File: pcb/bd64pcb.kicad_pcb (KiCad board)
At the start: 2 copper layers, 266.7 x 95.3 mm, 239 parts, among them J1 USB_C_Receptacle_USB2.0, J2 USB_B_Micro, SW1 SW_Push, U1 ATmega32U4-MU, U2 MCP23017_ML, U3 IS31FL3733-QF, Y1 16MHz

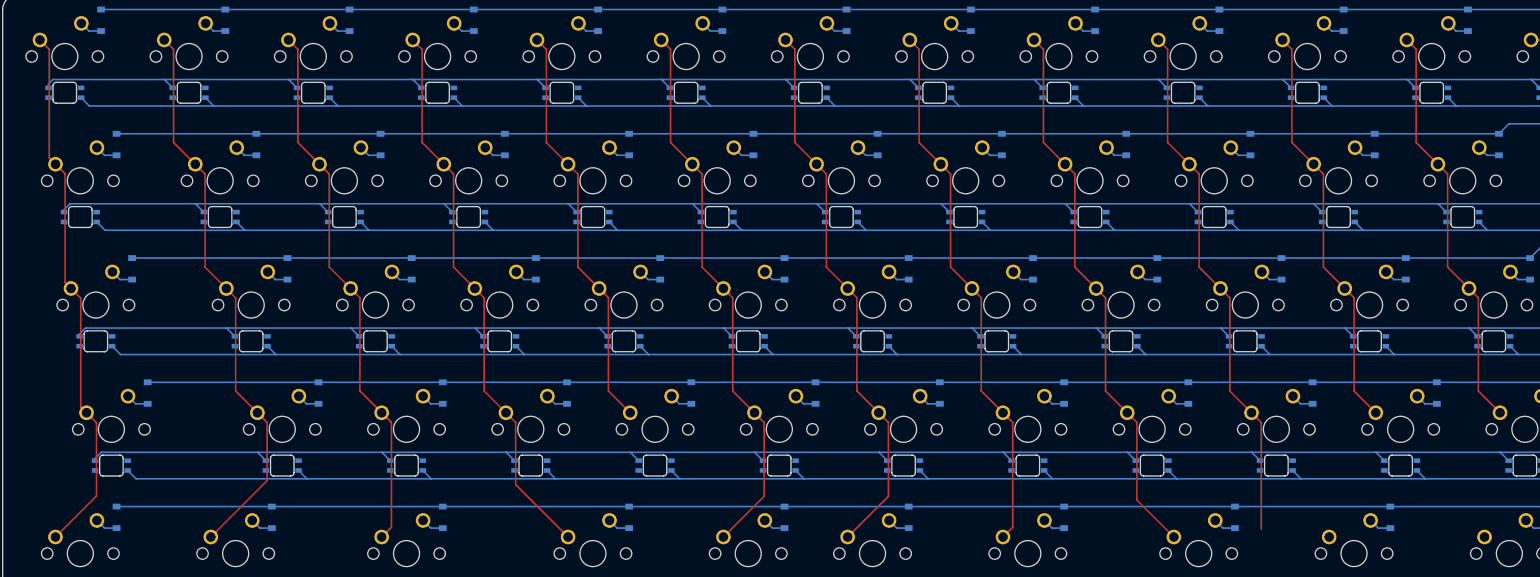
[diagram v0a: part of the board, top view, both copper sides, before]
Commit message: first non45 trace down
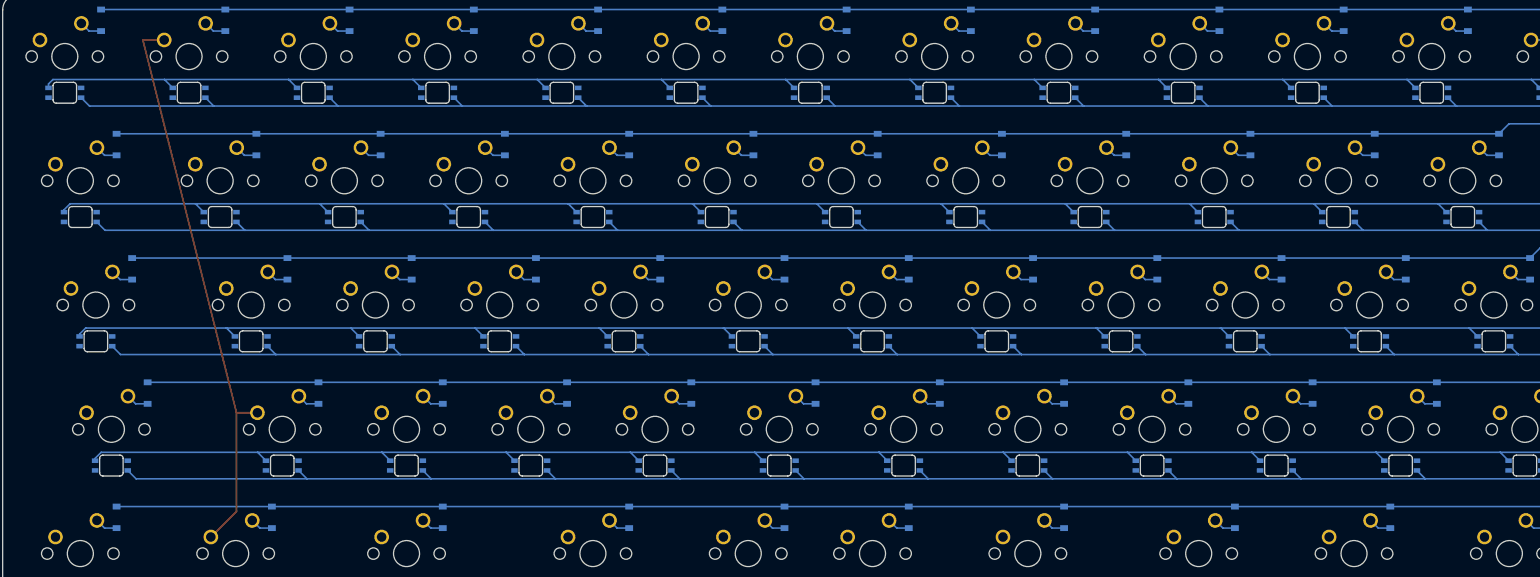
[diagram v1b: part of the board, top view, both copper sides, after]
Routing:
- net col3: track 86.1 -> 0.00 mm
- net col6: track 85.3 -> 0.00 mm
- net col5: track 85.3 -> 0.00 mm
- net col8: track 85.1 -> 0.00 mm
- net col2: track 83.4 -> 0.00 mm
- net col7: track 83.4 -> 0.00 mm
- net col0: track 82.4 -> 0.00 mm
- net col9: track 81.6 -> 0.00 mm
- net col10: track 63.1 -> 0.00 mm
- net col4: track 63.1 -> 0.00 mm
- net col11: track 63.1 -> 0.00 mm

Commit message: boring traces on most LEDs. updated to kicad 6
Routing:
- net col11: track 0.00 -> 102.1 mm, vias 0 -> 1
- net col10: track 0.00 -> 97.4 mm, vias 0 -> 1
- net col9: track 0.00 -> 92.6 mm, vias 0 -> 1
- net col3: track 0.00 -> 86.1 mm
- net col6: track 0.00 -> 85.2 mm
- net col5: track 0.00 -> 85.2 mm
- net col8: track 0.00 -> 85.1 mm
- net col7: track 0.00 -> 83.2 mm
- net col2: track 0.00 -> 83.2 mm
- net col0: track 0.00 -> 82.3 mm
- net CS9: track 0.00 -> 67.6 mm, vias 0 -> 4
- net CS7: track 0.00 -> 67.6 mm, vias 0 -> 4
- net CS12: track 0.00 -> 67.6 mm, vias 0 -> 4
- net CS10: track 0.00 -> 67.6 mm, vias 0 -> 4
- net CS5: track 0.00 -> 67.6 mm, vias 0 -> 4
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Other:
- board size 266.7 x 95.3 mm -> 266.7 x 95.2 mm
- net class Default removed
- net class Power removed

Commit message: still tracing LEDs
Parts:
- moved L48 209.4 mm to (198.4, 133.3)
- moved L47 202.3 mm to (172.2, 133.3)
- moved L46 197.6 mm to (148.4, 133.3)
- moved L32 152.7 mm to (129.4, 133.3)
- moved L31 148.1 mm to (105.6, 133.3)
- moved L30 138.8 mm to (77.0, 133.3)
- moved L16 74.1 mm to (50.8, 133.3)
- moved L15 72.3 mm to (27.0, 133.3)
- moved C9 14.4 mm to (52.8, 158.4), turned to -90 degrees
- moved JP6 13.2 mm to (52.8, 154.9), turned to 90 degrees
- moved C12 10.1 mm to (42.9, 159.1)
- moved C11 9.53 mm to (46.5, 159.1)
- moved C10 9.18 mm to (50.0, 159.1)
- moved C16 9.18 mm to (69.2, 184.2)
- moved C8 9.18 mm to (89.4, 155.1)
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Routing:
- net SW1: track 0.00 -> 286.7 mm, vias 0 -> 26
- net SW4: track 0.00 -> 274.9 mm, vias 0 -> 24
- net SW10: track 0.00 -> 274.9 mm, vias 0 -> 24
- net SW7: track 0.00 -> 274.2 mm, vias 0 -> 24
- net CS13: track 0.00 -> 44.6 mm, vias 0 -> 4

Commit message: shifted diodes over a tad
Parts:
- moved D61 6.51 mm to (197.5, 122.2)
- moved D62 6.51 mm to (221.3, 122.2)
- moved D63 6.51 mm to (245.1, 122.2)
- moved D64 6.51 mm to (268.9, 122.2)
- moved D10 6.35 mm to (195.3, 46.0)
- moved D14 6.35 mm to (271.5, 46.0)
- moved D25 6.35 mm to (219.1, 65.1)
- moved D34 6.35 mm to (147.6, 84.1)
- moved D39 6.35 mm to (242.9, 84.1)
- moved D40 6.35 mm to (266.7, 84.1)
- moved D48 6.35 mm to (171.4, 103.2)
- moved D59 6.35 mm to (147.6, 122.2)
- moved D60 6.35 mm to (171.4, 122.2)
- moved D17 6.35 mm to (66.7, 65.1)
- moved D18 6.35 mm to (85.7, 65.1)
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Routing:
- net row3: track 257.0 -> 216.8 mm, vias 2 -> 0
- net CS13: track 44.6 -> 74.5 mm, vias 4 -> 6
- net row4: track 265.2 -> 262.7 mm
- net row1: track 266.6 -> 264.6 mm
- net row2: track 257.0 -> 255.8 mm

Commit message: removed all traces. restarting
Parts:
- moved U1 126.0 mm to (44.0, 104.8), turned to 45 degrees
- moved F1 124.8 mm to (16.7, 31.0)
- moved JP1 122.8 mm to (24.4, 29.8)
- moved JP2 122.8 mm to (27.1, 29.8)
- moved R1 122.8 mm to (24.4, 33.2)
- moved R2 122.8 mm to (27.1, 33.2)
- moved J1 116.8 mm to (33.4, 46.4)
- moved U2 102.6 mm to (40.8, 85.7), turned to 45 degrees
- moved U3 54.3 mm to (91.3, 127.8), turned to 45 degrees
- moved R11 18.6 mm to (49.4, 153.7)
- moved C14 18.6 mm to (29.5, 153.7)
- moved C15 18.6 mm to (25.9, 153.7)
- moved C13 18.6 mm to (33.0, 153.7)
- moved JP7 18.6 mm to (47.9, 176.5)
- moved R10 18.6 mm to (54.9, 149.7)
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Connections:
- J1 pad A8: (no net) -> unconnected-(J1-PadA8)
- J1 pad B8: (no net) -> unconnected-(J1-PadB8)
- J2 pad 4: (no net) -> unconnected-(J2-Pad4)
- U1 pad 1: (no net) -> unconnected-(U1-Pad1)
- U1 pad 10: (no net) -> unconnected-(U1-Pad10)
- U1 pad 11: (no net) -> unconnected-(U1-Pad11)
- U1 pad 12: (no net) -> unconnected-(U1-Pad12)
- U1 pad 21: (no net) -> unconnected-(U1-Pad21)
- U1 pad 22: (no net) -> unconnected-(U1-Pad22)
- U1 pad 25: (no net) -> unconnected-(U1-Pad25)
- U1 pad 26: (no net) -> unconnected-(U1-Pad26)
- U1 pad 27: (no net) -> unconnected-(U1-Pad27)
- U1 pad 28: (no net) -> unconnected-(U1-Pad28)
- U1 pad 30: (no net) -> unconnected-(U1-Pad30)
- U1 pad 32: (no net) -> unconnected-(U1-Pad32)
- U1 pad 36: (no net) -> unconnected-(U1-Pad36)
- U1 pad 37: (no net) -> unconnected-(U1-Pad37)
- U1 pad 38: (no net) -> unconnected-(U1-Pad38)
- U1 pad 39: (no net) -> unconnected-(U1-Pad39)
- U1 pad 40: (no net) -> unconnected-(U1-Pad40)
- U1 pad 41: (no net) -> unconnected-(U1-Pad41)
- U1 pad 42: (no net) -> unconnected-(U1-Pad42)
- U1 pad 8: (no net) -> unconnected-(U1-Pad8)
- U1 pad 9: (no net) -> unconnected-(U1-Pad9)
- U2 pad 1: (no net) -> unconnected-(U2-Pad1)
- U2 pad 10: (no net) -> unconnected-(U2-Pad10)
- U2 pad 15: (no net) -> unconnected-(U2-Pad15)
- U2 pad 16: (no net) -> unconnected-(U2-Pad16)
- U2 pad 17: (no net) -> unconnected-(U2-Pad17)
- U2 pad 18: (no net) -> unconnected-(U2-Pad18)
- U2 pad 19: (no net) -> unconnected-(U2-Pad19)
- U2 pad 2: (no net) -> unconnected-(U2-Pad2)
- U2 pad 20: (no net) -> unconnected-(U2-Pad20)
- U2 pad 21: (no net) -> unconnected-(U2-Pad21)
- U2 pad 22: (no net) -> unconnected-(U2-Pad22)
- U2 pad 23: (no net) -> unconnected-(U2-Pad23)
- U2 pad 24: (no net) -> unconnected-(U2-Pad24)
- U2 pad 25: (no net) -> unconnected-(U2-Pad25)
- U2 pad 26: (no net) -> unconnected-(U2-Pad26)
- U2 pad 27: (no net) -> unconnected-(U2-Pad27)
- U2 pad 28: (no net) -> unconnected-(U2-Pad28)
- U2 pad 3: (no net) -> unconnected-(U2-Pad3)
- U2 pad 4: (no net) -> unconnected-(U2-Pad4)
- U2 pad 7: (no net) -> unconnected-(U2-Pad7)
- U3 pad 1: (no net) -> unconnected-(U3-Pad1)
- U3 pad 36: (no net) -> unconnected-(U3-Pad36)
- U3 pad 40: (no net) -> unconnected-(U3-Pad40)
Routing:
- net SW1: track 286.7 -> 0.00 mm, vias 26 -> 0
- net SW4: track 274.9 -> 0.00 mm, vias 24 -> 0
- net SW10: track 274.9 -> 0.00 mm, vias 24 -> 0
- net SW7: track 274.2 -> 0.00 mm, vias 24 -> 0
- net SW2: track 270.8 -> 0.00 mm
- net SW3: track 270.8 -> 0.00 mm
- net row1: track 264.6 -> 0.00 mm, vias 2 -> 0
- net row4: track 262.7 -> 0.00 mm, vias 2 -> 0
- net SW8: track 259.5 -> 0.00 mm
- net SW5: track 259.5 -> 0.00 mm
- net SW11: track 259.5 -> 0.00 mm
- net SW9: track 259.3 -> 0.00 mm
- net SW6: track 259.3 -> 0.00 mm
- net SW12: track 259.3 -> 0.00 mm
- net row2: track 255.8 -> 0.00 mm, vias 2 -> 0
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
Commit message: curves in progress
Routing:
- net SW6: track 0.00 -> 306.1 mm, vias 0 -> 28
- net SW3: track 0.00 -> 303.1 mm, vias 0 -> 28
- net SW4: track 0.00 -> 279.8 mm
- net SW1: track 0.00 -> 276.8 mm
- net SW5: track 0.00 -> 274.4 mm
- net SW2: track 0.00 -> 271.4 mm
- net col11: track 0.00 -> 148.3 mm
- net col2: track 0.00 -> 94.8 mm
- net col7: track 0.00 -> 91.5 mm
- net col9: track 0.00 -> 75.8 mm
- net col5: track 0.00 -> 75.8 mm
- net col4: track 0.00 -> 75.8 mm
- net col3: track 0.00 -> 75.8 mm
- net col8: track 0.00 -> 75.8 mm
- net col6: track 0.00 -> 75.8 mm
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
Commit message: easy LEDs routed
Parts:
- moved U1 133.5 mm to (151.1, 184.4)
- moved U2 104.2 mm to (94.9, 174.8)
- moved U3 82.6 mm to (46.0, 196.8)
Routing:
- net SW9: track 0.00 -> 248.2 mm, vias 0 -> 22
- net SW12: track 0.00 -> 244.5 mm, vias 0 -> 22
- net SW7: track 0.00 -> 227.6 mm
- net SW8: track 0.00 -> 227.3 mm
- net SW11: track 0.00 -> 224.2 mm
- net SW10: track 0.00 -> 223.8 mm
- net col11: track 148.3 -> 72.5 mm
- net col1: track 0.00 -> 75.8 mm
- net CS9: track 25.7 -> 71.0 mm, vias 2 -> 4
- net CS3: track 25.7 -> 71.0 mm, vias 2 -> 4
- net CS11: track 25.7 -> 71.0 mm, vias 2 -> 4
- net CS10: track 25.7 -> 71.0 mm, vias 2 -> 4
- net CS6: track 25.7 -> 71.0 mm, vias 2 -> 4
- net CS4: track 25.7 -> 71.0 mm, vias 2 -> 4
- net CS7: track 25.7 -> 71.0 mm, vias 2 -> 4
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
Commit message: easy diodes routed
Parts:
- moved D54 5.08 mm to (26.2, 123.0), turned to 90 degrees
- moved D55 5.08 mm to (50.0, 123.0), turned to 90 degrees
- moved D28 4.27 mm to (28.6, 84.9), turned to 90 degrees
- moved D41 4.27 mm to (31.0, 104.0), turned to 90 degrees
- moved D29 4.27 mm to (52.4, 84.9), turned to 90 degrees
- moved D42 4.27 mm to (57.1, 104.0), turned to 90 degrees
- moved D56 4.27 mm to (76.2, 123.0), turned to 90 degrees
- moved D57 4.27 mm to (104.8, 123.0), turned to 90 degrees
- moved D61 0.81 mm to (197.6, 123.0), turned to 90 degrees
- moved D62 0.81 mm to (221.5, 123.0), turned to 90 degrees
- moved D63 0.81 mm to (245.3, 123.0), turned to 90 degrees
- moved D64 0.81 mm to (269.1, 123.0), turned to 90 degrees
- moved D30 0.79 mm to (71.4, 84.9), turned to 90 degrees
- moved D31 0.79 mm to (90.5, 84.9), turned to 90 degrees
- moved D32 0.79 mm to (109.5, 84.9), turned to 90 degrees
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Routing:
- net row0: track 0.00 -> 361.6 mm
- net row1: track 0.00 -> 314.2 mm
- net row2: track 0.00 -> 289.6 mm
- net row3: track 0.00 -> 289.6 mm
- net SW2: track 271.4 -> 284.7 mm
- net SW3: track 303.1 -> 311.9 mm
- net SW1: track 276.8 -> 285.6 mm
- net SW5: track 274.4 -> 278.6 mm
- net Net-(D64-Pad2): track 0.00 -> 3.89 mm
- net Net-(D60-Pad2): track 0.00 -> 3.89 mm
- net Net-(D59-Pad2): track 0.00 -> 3.89 mm
- net Net-(D53-Pad2): track 0.00 -> 3.89 mm
- net Net-(D55-Pad2): track 0.00 -> 3.89 mm
- net Net-(D8-Pad2): track 0.00 -> 3.89 mm
- net Net-(D13-Pad2): track 0.00 -> 3.89 mm
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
